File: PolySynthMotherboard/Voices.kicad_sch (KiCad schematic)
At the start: 23 parts, among them U401 TCA9548APWR, U402 Voice1, U403 Voice2, U404 Voice3, U405 Voice4, U406 Voice5, U407 Voice6

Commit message: motherboard rev1
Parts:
- removed U402: Voice1, Connector_PinHeader_2.54mm:PinHeader_2x09_P2.54mm_Vertical, symbol Connector_Audio:VoiceBoardConn_18P_254P
- removed U403: Voice2, Connector_PinHeader_2.54mm:PinHeader_2x09_P2.54mm_Vertical, symbol Connector_Audio:VoiceBoardConn_18P_254P
- removed U404: Voice3, Connector_PinHeader_2.54mm:PinHeader_2x09_P2.54mm_Vertical, symbol Connector_Audio:VoiceBoardConn_18P_254P
- removed U405: Voice4, Connector_PinHeader_2.54mm:PinHeader_2x09_P2.54mm_Vertical, symbol Connector_Audio:VoiceBoardConn_18P_254P
- removed U406: Voice5, Connector_PinHeader_2.54mm:PinHeader_2x09_P2.54mm_Vertical, symbol Connector_Audio:VoiceBoardConn_18P_254P
- removed U407: Voice6, Connector_PinHeader_2.54mm:PinHeader_2x09_P2.54mm_Vertical, symbol Connector_Audio:VoiceBoardConn_18P_254P
- added U402: V1, Package_DIP:DIP-18_W7.62mm_Socket, symbol Connector_Audio:VoiceBoardConn_DIP18
- added U403: V2, Package_DIP:DIP-18_W7.62mm_Socket, symbol Connector_Audio:VoiceBoardConn_DIP18
- added U404: V3, Package_DIP:DIP-18_W7.62mm_Socket, symbol Connector_Audio:VoiceBoardConn_DIP18
- added U405: V4, Package_DIP:DIP-18_W7.62mm_Socket, symbol Connector_Audio:VoiceBoardConn_DIP18
- added U406: V5, Package_DIP:DIP-18_W7.62mm_Socket, symbol Connector_Audio:VoiceBoardConn_DIP18
- added U407: V6, Package_DIP:DIP-18_W7.62mm_Socket, symbol Connector_Audio:VoiceBoardConn_DIP18
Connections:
- net +12V: now also U402.9 (+12V), U403.9 (+12V), U404.9 (+12V), U405.9 (+12V), U406.9 (+12V), U407.9 (+12V)
- net +3.3V: now also U402.8 (+3V3), U403.8 (+3V3), U404.8 (+3V3), U405.8 (+3V3), U406.8 (+3V3), U407.8 (+3V3)
- net -12V: now also U402.10 (-12V), U403.10 (-12V), U404.10 (-12V), U405.10 (-12V), U406.10 (-12V), U407.10 (-12V)
- net CUTOFF_V1: now also U402.13 (VCF)
- net CUTOFF_V2: now also U403.13 (VCF)
- net CUTOFF_V3: now also U404.13 (VCF)
- net CUTOFF_V4: now also U405.13 (VCF)
- net CUTOFF_V5: now also U406.13 (VCF)
- net CUTOFF_V6: now also U407.13 (VCF)
- net FOLD_FIRST: now also U402.6 (FF), U403.6 (FF), U404.6 (FF), U405.6 (FF), U406.6 (FF), U407.6 (FF)
- net FOLD_V1: now also U402.14 (FOLD)
- net FOLD_V2: now also U403.14 (FOLD)
- net FOLD_V3: now also U404.14 (FOLD)
- net FOLD_V4: now also U405.14 (FOLD)
- net FOLD_V5: now also U406.14 (FOLD)
- net FOLD_V6: now also U407.14 (FOLD)
- net GND: now also U402.11 (GND), U403.11 (GND), U404.11 (GND), U405.11 (GND), U406.11 (GND), U407.11 (GND)
- net HP_MODE: now also U402.5 (HP), U403.5 (HP), U404.5 (HP), U405.5 (HP), U406.5 (HP), U407.5 (HP)
- net LVL1_V1: now also U402.18 (LVL1)
- net LVL1_V2: now also U403.18 (LVL1)
- net LVL1_V3: now also U404.18 (LVL1)
- net LVL1_V4: now also U405.18 (LVL1)
- net LVL1_V5: now also U406.18 (LVL1)
- net LVL1_V6: now also U407.18 (LVL1)
- net LVL2_V1: now also U402.17 (LVL2)
- net LVL2_V2: now also U403.17 (LVL2)
- net LVL2_V3: now also U404.17 (LVL2)
- net LVL2_V4: now also U405.17 (LVL2)
- net LVL2_V5: now also U406.17 (LVL2)
- net LVL2_V6: now also U407.17 (LVL2)
- net PWM1_V1: now also U402.16 (PWM1)
- net PWM1_V2: now also U403.16 (PWM1)
- net PWM1_V3: now also U404.16 (PWM1)
- net PWM1_V4: now also U405.16 (PWM1)
- net PWM1_V5: now also U406.16 (PWM1)
- net PWM1_V6: now also U407.16 (PWM1)
- net PWM2_V1: now also U402.15 (PWM2)
- net PWM2_V2: now also U403.15 (PWM2)
- net PWM2_V3: now also U404.15 (PWM2)
- net PWM2_V4: now also U405.15 (PWM2)
- net PWM2_V5: now also U406.15 (PWM2)
- net PWM2_V6: now also U407.15 (PWM2)
- net SCL_V1: now also U402.2 (SCL)
- net SCL_V2: now also U403.2 (SCL)
- net SCL_V3: now also U404.2 (SCL)
- net SCL_V4: now also U405.2 (SCL)
- net SCL_V5: now also U406.2 (SCL)
- net SCL_V6: now also U407.2 (SCL)
- net SDA_V1: now also U402.1 (SDA)
- net SDA_V2: now also U403.1 (SDA)
- net SDA_V3: now also U404.1 (SDA)
- net SDA_V4: now also U405.1 (SDA)
- net SDA_V5: now also U406.1 (SDA)
- net SDA_V6: now also U407.1 (SDA)
- net V1_CLK1: now also U402.3 (CLK1)
- net V1_CLK2: now also U402.4 (CLK2)
- net V1_OUT: now also U402.7 (OUT)
- net V2_CLK1: now also U403.3 (CLK1)
- net V2_CLK2: now also U403.4 (CLK2)
- net V2_OUT: now also U403.7 (OUT)
- net V3_CLK1: now also U404.3 (CLK1)
- net V3_CLK2: now also U404.4 (CLK2)
- net V3_OUT: now also U404.7 (OUT)
- net V4_CLK1: now also U405.3 (CLK1)
- net V4_CLK2: now also U405.4 (CLK2)
- net V4_OUT: now also U405.7 (OUT)
- net V5_CLK1: now also U406.3 (CLK1)
- net V5_CLK2: now also U406.4 (CLK2)
- net V5_OUT: now also U406.7 (OUT)
- net V6_CLK1: now also U407.3 (CLK1)
- net V6_CLK2: now also U407.4 (CLK2)
- net V6_OUT: now also U407.7 (OUT)
- net VCA_V1: now also U402.12 (VCA)
- net VCA_V2: now also U403.12 (VCA)
- net VCA_V3: now also U404.12 (VCA)
- net VCA_V4: now also U405.12 (VCA)
- net VCA_V5: now also U406.12 (VCA)
- net VCA_V6: now also U407.12 (VCA)

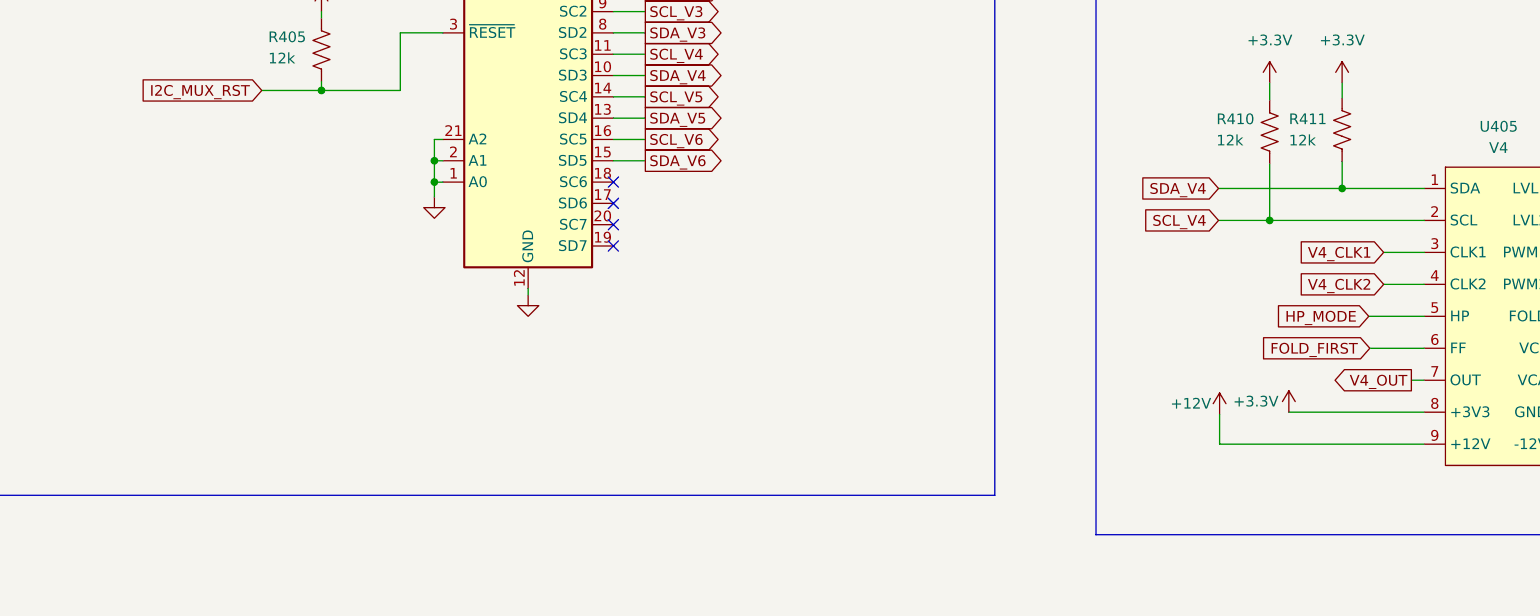
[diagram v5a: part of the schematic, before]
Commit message: updated to kicad 8
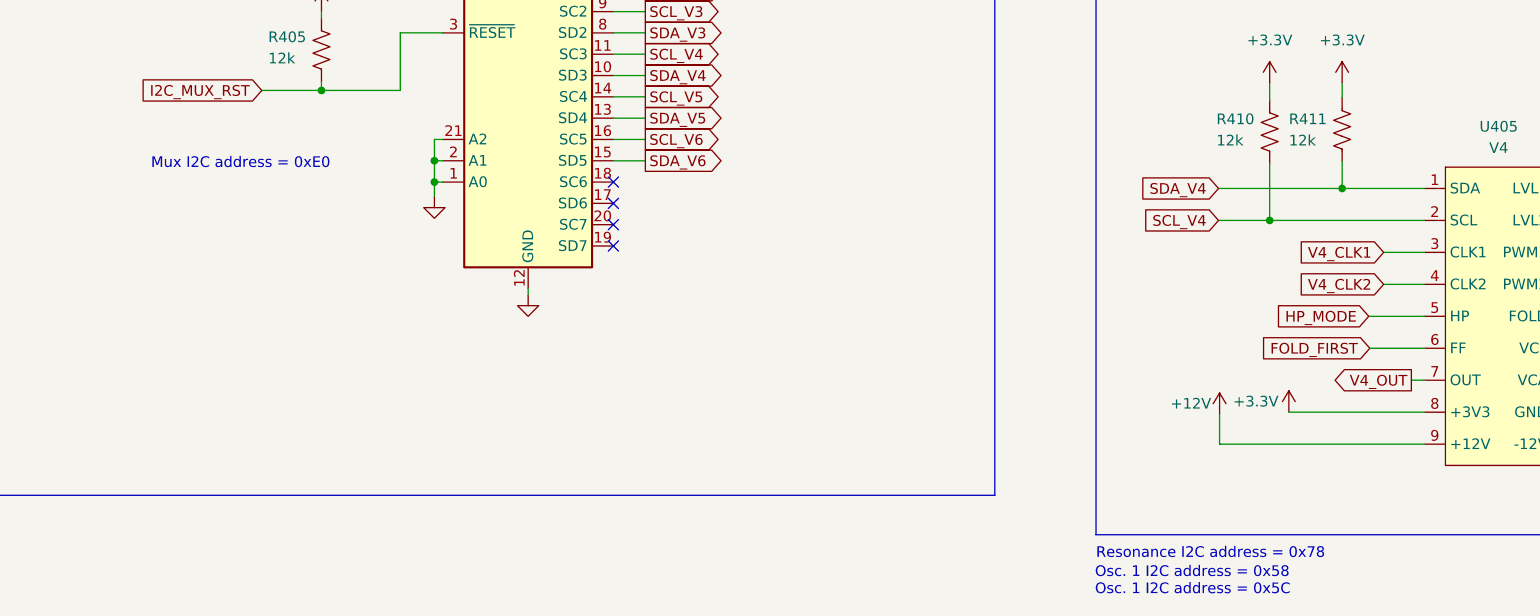
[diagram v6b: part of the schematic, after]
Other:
- note added: "Mux I2C address = 0xE0"
- note added: "Osc. 1 I2C address = 0x58 Osc. 1 I2C address = 0x5C"
- note added: "Resonance I2C address = 0x78"

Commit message: fixed footprints, switched optocoupler
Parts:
- R401, R402, R403, R404, R405, R406, R407, R408, R409, R410, R411, R412, R413, R414, R415: footprint PCM_Resistor_SMD_AKL:R_0805_2012Metric -> Resistor_SMD:R_0805_2012Metric
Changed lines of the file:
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@@
 			)
 		)
-		(property "Footprint" "PCM_Resistor_SMD_AKL:R_0805_2012Metric"
+		(property "Footprint" "Resistor_SMD:R_0805_2012Metric"
 			(at 74.168 111.252 90)
 			(effects
@@
 			)
 		)
-		(property "Footprint" "PCM_Resistor_SMD_AKL:R_0805_2012Metric"
+		(property "Footprint" "Resistor_SMD:R_0805_2012Metric"
 			(at 319.024 145.161 90)
 			(effects
@@
 			)
 		)
-		(property "Footprint" "PCM_Resistor_SMD_AKL:R_0805_2012Metric"
+		(property "Footprint" "Resistor_SMD:R_0805_2012Metric"
 			(at 63.246 111.506 90)
 			(effects
@@
 			)
 		)
-		(property "Footprint" "PCM_Resistor_SMD_AKL:R_0805_2012Metric"
+		(property "Footprint" "Resistor_SMD:R_0805_2012Metric"
 			(at 327.66 144.907 90)
 			(effects
@@
 			)
 		)
-		(property "Footprint" "PCM_Resistor_SMD_AKL:R_0805_2012Metric"
+		(property "Footprint" "Resistor_SMD:R_0805_2012Metric"
 			(at 180.34 145.669 90)
 			(effects
@@
 			)
 		)
-		(property "Footprint" "PCM_Resistor_SMD_AKL:R_0805_2012Metric"
+		(property "Footprint" "Resistor_SMD:R_0805_2012Metric"
 			(at 178.181 84.201 90)
 			(effects
@@
 			)
 		)
-		(property "Footprint" "PCM_Resistor_SMD_AKL:R_0805_2012Metric"
+		(property "Footprint" "Resistor_SMD:R_0805_2012Metric"
 			(at 250.571 145.415 90)
 			(effects
@@
 			)
 		)
-		(property "Footprint" "PCM_Resistor_SMD_AKL:R_0805_2012Metric"
+		(property "Footprint" "Resistor_SMD:R_0805_2012Metric"
 			(at 325.501 83.439 90)
 			(effects
@@
 			)
 		)
-		(property "Footprint" "PCM_Resistor_SMD_AKL:R_0805_2012Metric"
+		(property "Footprint" "Resistor_SMD:R_0805_2012Metric"
 			(at 316.865 83.693 90)
 			(effects
@@
 			)
 		)
-		(property "Footprint" "PCM_Resistor_SMD_AKL:R_0805_2012Metric"
+		(property "Footprint" "Resistor_SMD:R_0805_2012Metric"
 			(at 257.048 83.693 90)
 			(effects
@@
 			)
 		)
-		(property "Footprint" "PCM_Resistor_SMD_AKL:R_0805_2012Metric"
+		(property "Footprint" "Resistor_SMD:R_0805_2012Metric"
 			(at 248.412 83.947 90)
 			(effects
@@
 			)
 		)
-		(property "Footprint" "PCM_Resistor_SMD_AKL:R_0805_2012Metric"
+		(property "Footprint" "Resistor_SMD:R_0805_2012Metric"
 			(at 188.976 145.415 90)
 			(effects
@@
 			)
 		)
-		(property "Footprint" "PCM_Resistor_SMD_AKL:R_0805_2012Metric"
+		(property "Footprint" "Resistor_SMD:R_0805_2012Metric"
 			(at 186.817 83.947 90)
 			(effects
@@
 			)
 		)
-		(property "Footprint" "PCM_Resistor_SMD_AKL:R_0805_2012Metric"
+		(property "Footprint" "Resistor_SMD:R_0805_2012Metric"
 			(at 259.207 145.161 90)
 			(effects
@@
 			)
 		)
-		(property "Footprint" "PCM_Resistor_SMD_AKL:R_0805_2012Metric"
+		(property "Footprint" "Resistor_SMD:R_0805_2012Metric"
 			(at 67.31 135.89 90)
 			(effects

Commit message: voice board rev4
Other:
- note added: "Osc. 1 I2C address = 0x58 Osc. 2 I2C address = 0x5C"
- note added: "Resonance I2C address = 0x5A*"
- note removed: "Osc. 1 I2C address = 0x58 Osc. 1 I2C address = 0x5C"
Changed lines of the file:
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@@
 		)
 	)
-	(text "Osc. 1 I2C address = 0x58\nOsc. 1 I2C address = 0x5C"
+	(text "Osc. 1 I2C address = 0x58\nOsc. 2 I2C address = 0x5C"
 		(exclude_from_sim no)
 		(at 158.496 200.787 0)
@@
 		)
 	)
+	(text "Resonance I2C address = 0x5A*"
+		(exclude_from_sim no)
+		(at 158.496 202.946 0)
+		(effects
+			(font
+				(size 1.27 1.27)
+			)
+			(justify left bottom)
+		)
+	)
 	(text "Mux I2C address = 0xE0"
 		(exclude_from_sim no)
@@
 		)
 	)
+	(sheet_instances
+		(path "/"
+			(page "1")
+		)
+	)
